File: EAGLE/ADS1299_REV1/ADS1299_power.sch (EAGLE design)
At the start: 12 parts

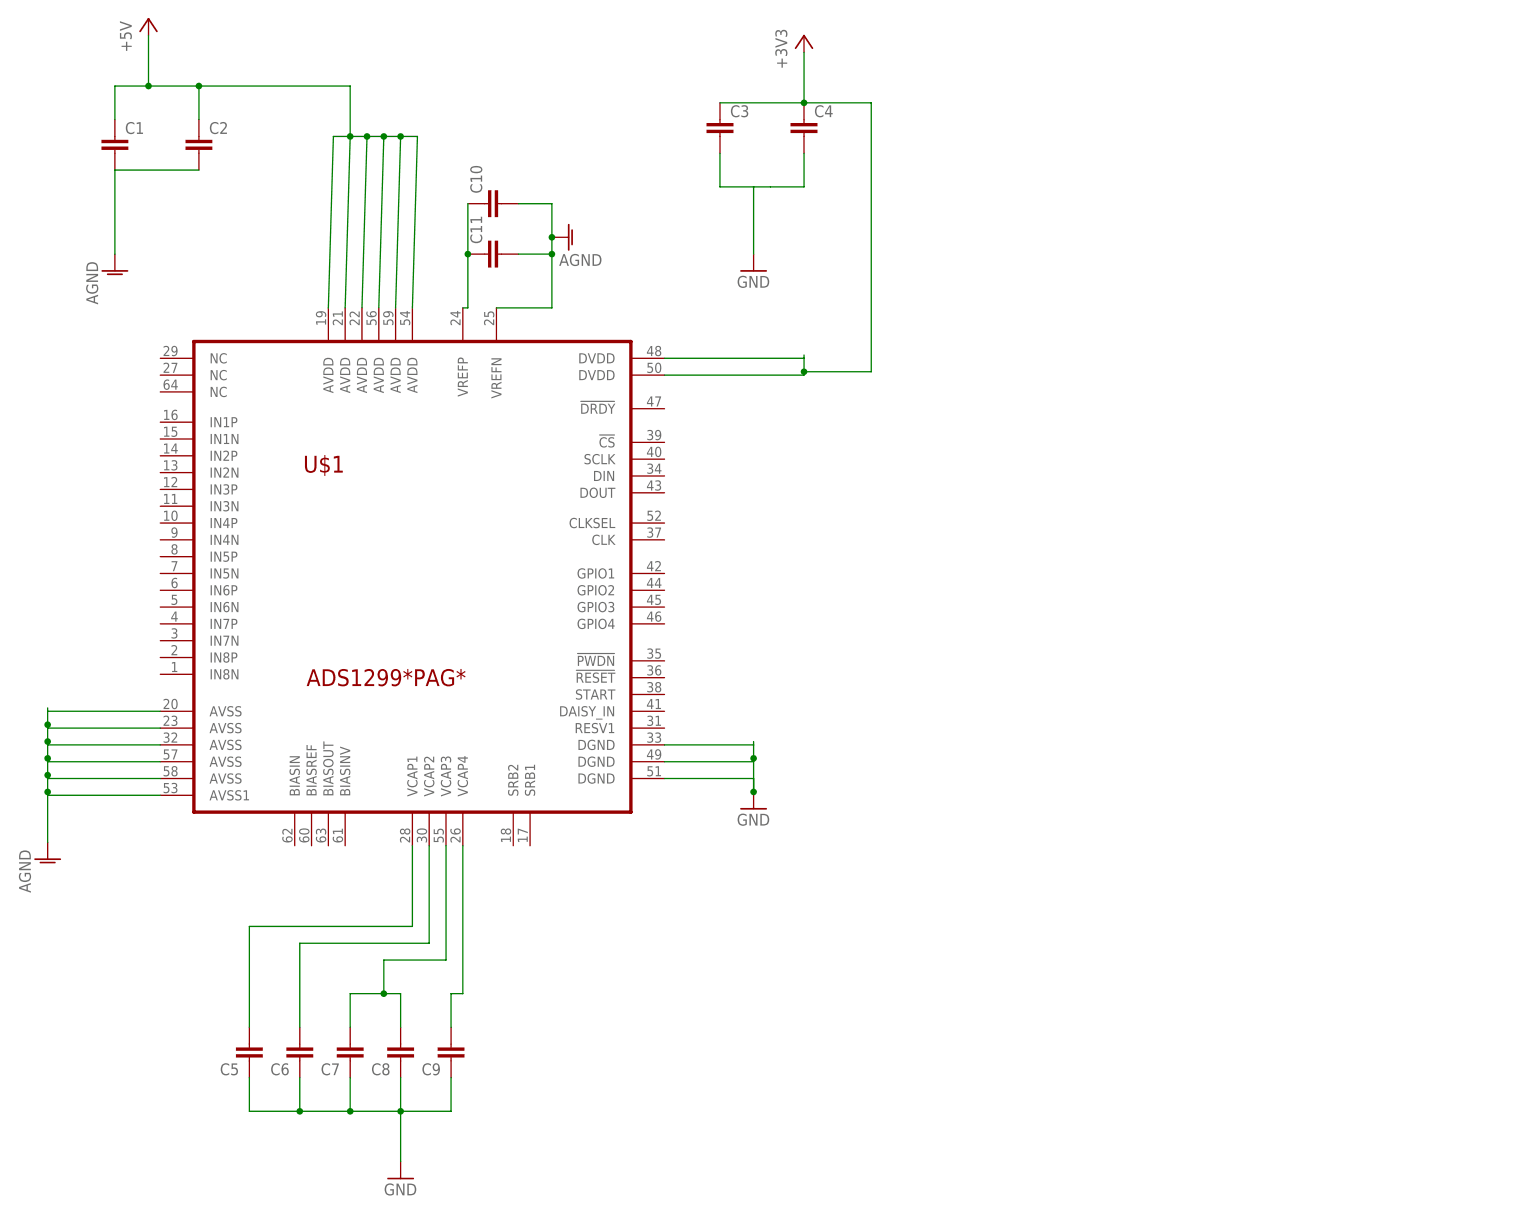
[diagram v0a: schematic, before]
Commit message: Added connections for all Digital pins (entire right side of chip)
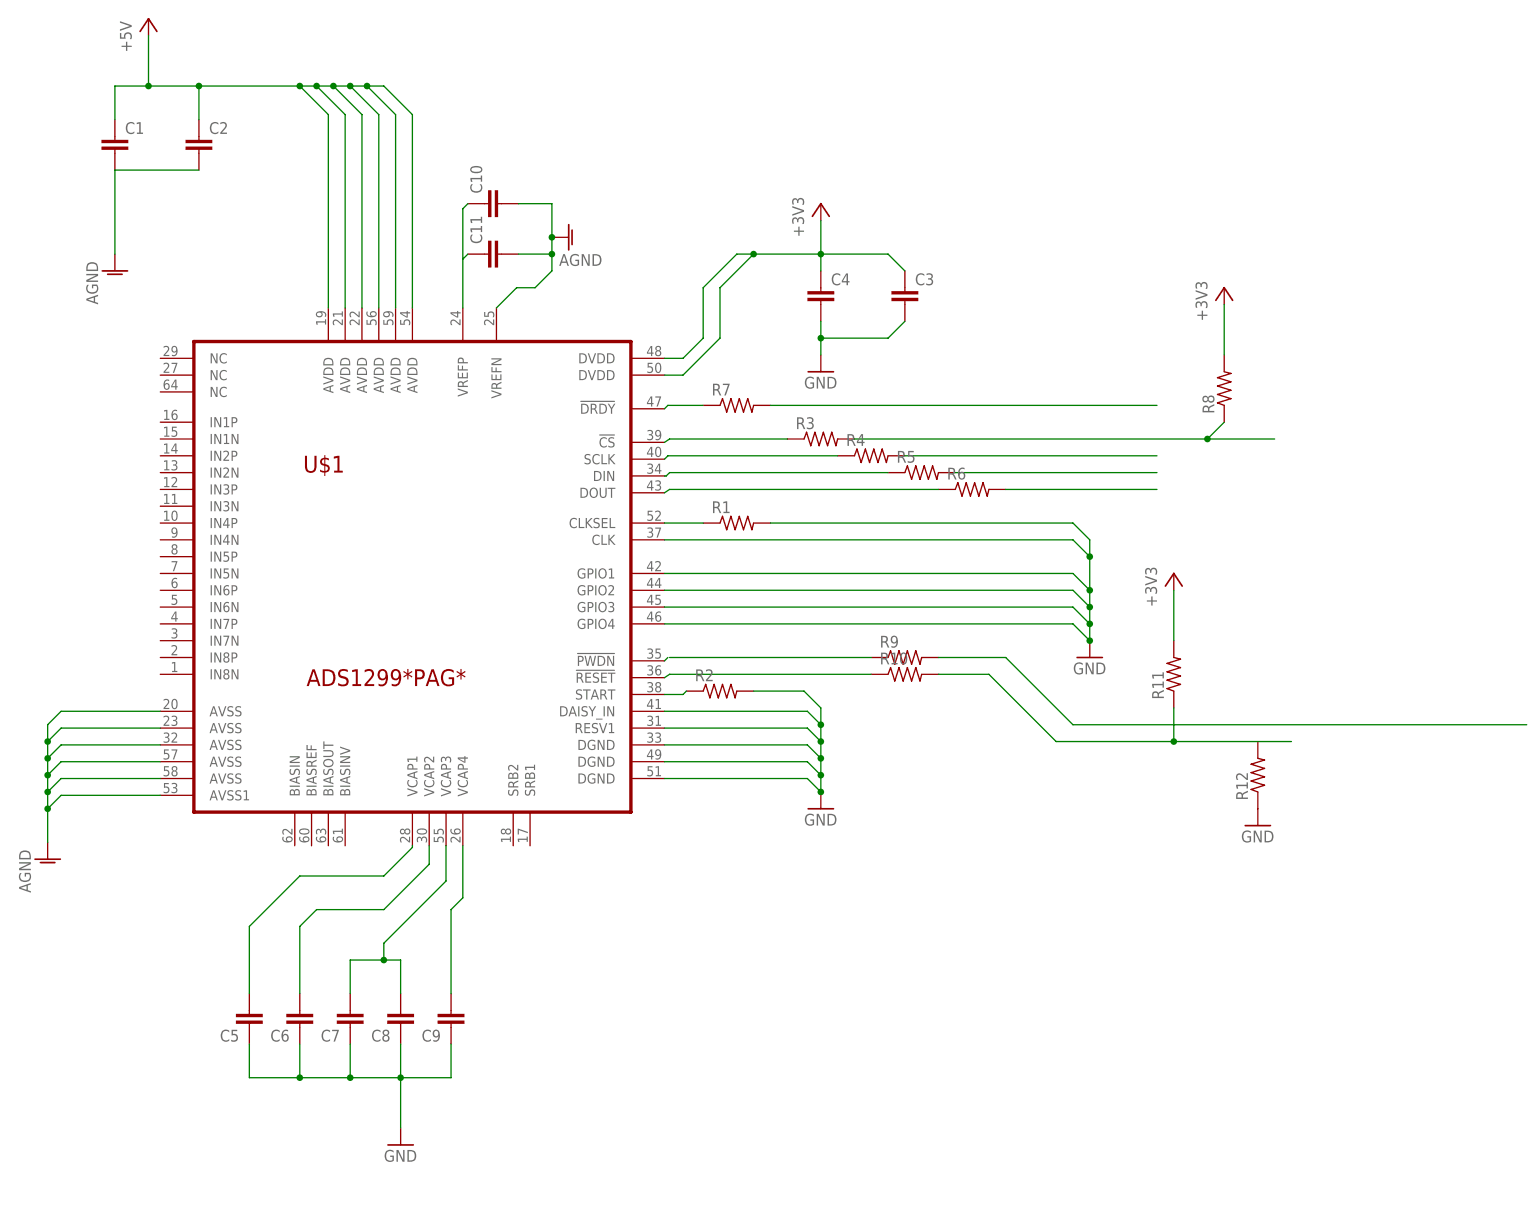
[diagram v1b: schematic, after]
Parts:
- added R1, R10, R11, R12, R2, R3, R4, R5, R6, R7, R8, R9: (no value), resistor:R-US_0204/2V
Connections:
- new net N$10: R2.1, U$1.START
- new net N$11: R5.1, U$1.DIN
- new net N$12: R6.1, U$1.DOUT
- new net N$13: R3.2, R8.1
- new net N$14: R4.2
- new net N$15: R5.2
- new net N$16: R6.2
- new net N$17: R7.1, U$1.!DRDY
- new net N$18: R7.2
- new net N$19: R10.1, U$1.!RESET
- new net N$20: U$1.!PWDN
- new net N$21: R9.1
- new net N$22: R10.2, R11.1
- new net N$23: R9.2
- new net N$4: R1.1, U$1.CLKSEL
- new net N$7: U$1.!CS
- new net N$8: R4.1, U$1.SCLK
- net +3V3: now also R11.2, R8.2
- net GND: now also R1.2, R2.2, U$1.CLK, U$1.DAISY_IN, U$1.GPIO1, U$1.GPIO2, U$1.GPIO3, U$1.GPIO4, U$1.RESV1
- net N$3: no longer C11.1
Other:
- moved on the sheet: C3, C4, C5, C6, C7, C8, C9
